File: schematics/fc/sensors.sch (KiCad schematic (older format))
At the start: 126 parts

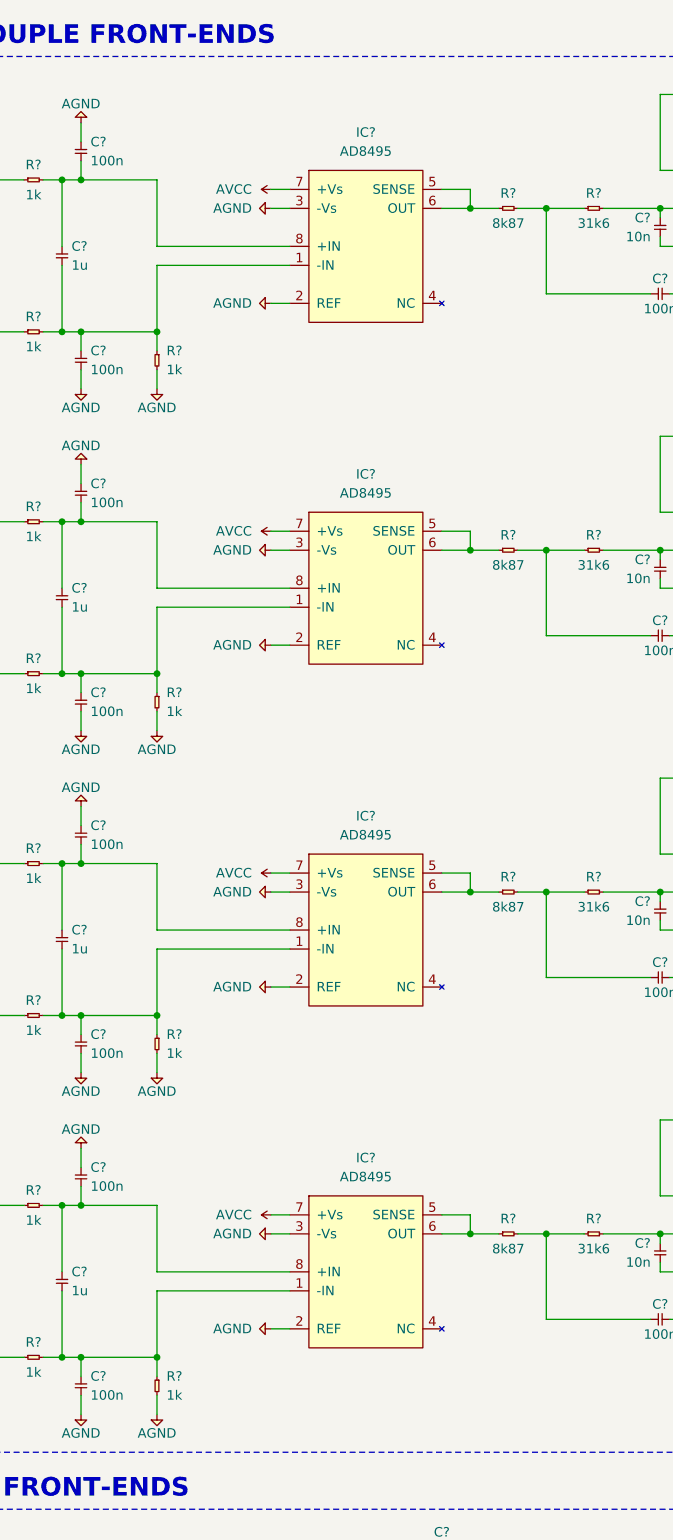
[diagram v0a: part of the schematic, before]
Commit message: Fix thermocouple grounding resistor values
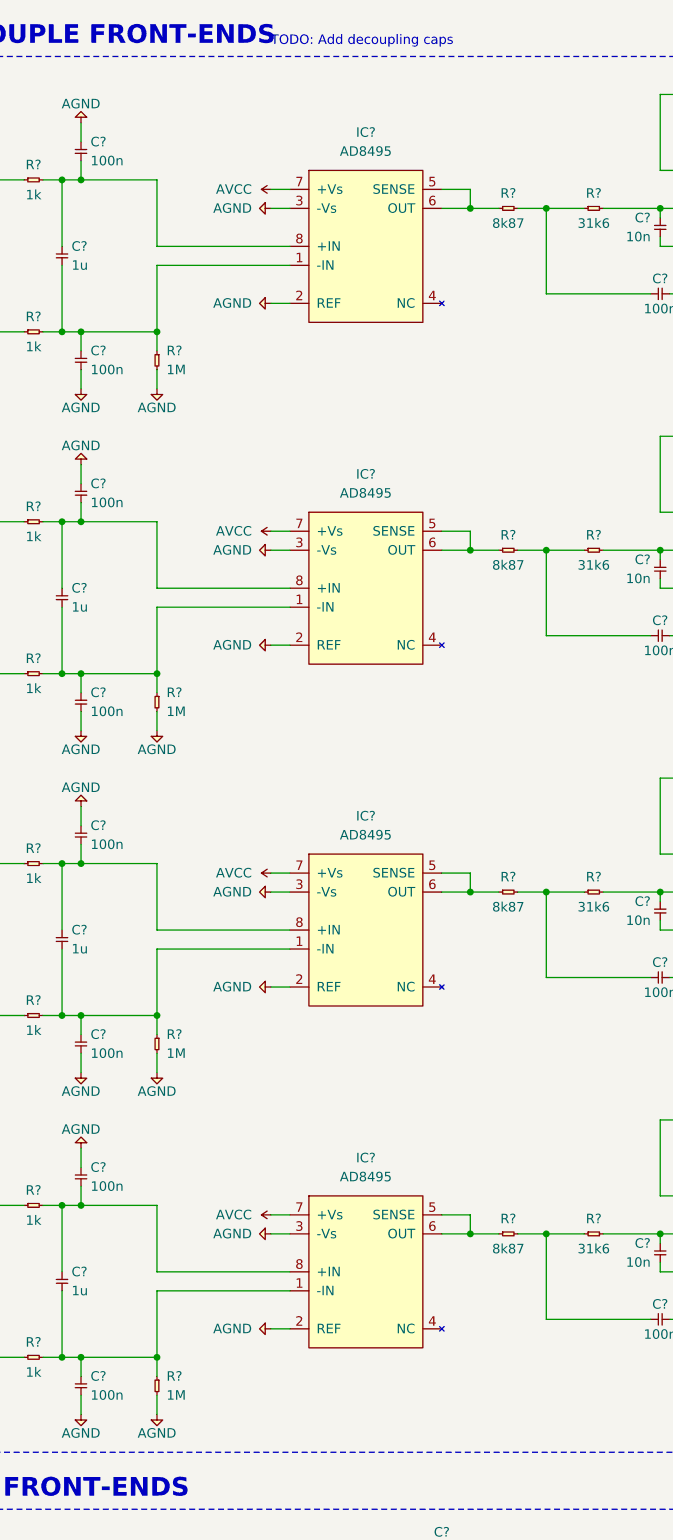
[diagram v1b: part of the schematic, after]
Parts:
- removed R? (x3): 1k, symbol cusf-kicad:R
- added R? (x3): 1M, symbol cusf-kicad:R
- R?: value 1k -> 1M
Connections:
- net AGND: now also R?.2, R?.2, R?.2
- net at C?.1, C?.2, IC?.1 (-IN)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: now also R?.1 (x3)
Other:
- note added: "TODO: Add decoupling caps"
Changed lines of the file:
@@
 Connection ~ 6050 2200
-$Comp
-L cusf-kicad:R R?
-U 1 1 613737F8
-P 6050 2300
-F 0 "R?" V 6050 2350 50  0000 L CNN
-F 1 "1k" V 6150 2350 50  0000 L CNN
-F 2 "" H 6050 2300 50  0001 C CNN
-F 3 "" H 6050 2300 50  0001 C CNN
-	1    6050 2300
-	0    1    1    0
-$EndComp
 $Comp
 L cusf-kicad:AGND #PWR?
@@
 Connection ~ 6050 4000
 $Comp
-L cusf-kicad:R R?
-U 1 1 616FFB57
-P 6050 4100
-F 0 "R?" V 6050 4150 50  0000 L CNN
-F 1 "1k" V 6150 4150 50  0000 L CNN
-F 2 "" H 6050 4100 50  0001 C CNN
-F 3 "" H 6050 4100 50  0001 C CNN
-	1    6050 4100
-	0    1    1    0
-$EndComp
-$Comp
 L cusf-kicad:AGND #PWR?
 U 1 1 616FFB5D
@@
 P 6050 5900
 F 0 "R?" V 6050 5950 50  0000 L CNN
-F 1 "1k" V 6150 5950 50  0000 L CNN
+F 1 "1M" V 6150 5950 50  0000 L CNN
 F 2 "" H 6050 5900 50  0001 C CNN
 F 3 "" H 6050 5900 50  0001 C CNN
@@
 	6050 7600 6050 7700
 Connection ~ 6050 7600
-$Comp
-L cusf-kicad:R R?
-U 1 1 618AFA1F
-P 6050 7700
-F 0 "R?" V 6050 7750 50  0000 L CNN
-F 1 "1k" V 6150 7750 50  0000 L CNN
-F 2 "" H 6050 7700 50  0001 C CNN
-F 3 "" H 6050 7700 50  0001 C CNN
-	1    6050 7700
-	0    1    1    0
-$EndComp
 $Comp
 L cusf-kicad:AGND #PWR?
@@
 	1    0    0    1
 $EndComp
+$Comp
+L cusf-kicad:R R?
+U 1 1 60817C8F
+P 6050 4100
+F 0 "R?" V 6050 4150 50  0000 L CNN
+F 1 "1M" V 6150 4150 50  0000 L CNN
+F 2 "" H 6050 4100 50  0001 C CNN
+F 3 "" H 6050 4100 50  0001 C CNN
+	1    6050 4100
+	0    1    1    0
+$EndComp
+$Comp
+L cusf-kicad:R R?
+U 1 1 60818006
+P 6050 2300
+F 0 "R?" V 6050 2350 50  0000 L CNN
+F 1 "1M" V 6150 2350 50  0000 L CNN
+F 2 "" H 6050 2300 50  0001 C CNN
+F 3 "" H 6050 2300 50  0001 C CNN
+	1    6050 2300
+	0    1    1    0
+$EndComp
+Text Notes 6650 700  0    50   ~ 0
+TODO: Add decoupling caps
+$Comp
+L cusf-kicad:R R?
+U 1 1 6081D011
+P 6050 7700
+F 0 "R?" V 6050 7750 50  0000 L CNN
+F 1 "1M" V 6150 7750 50  0000 L CNN
+F 2 "" H 6050 7700 50  0001 C CNN
+F 3 "" H 6050 7700 50  0001 C CNN
+	1    6050 7700
+	0    1    1    0
+$EndComp
 $EndSCHEMATC
